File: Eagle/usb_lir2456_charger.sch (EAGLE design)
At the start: 14 parts

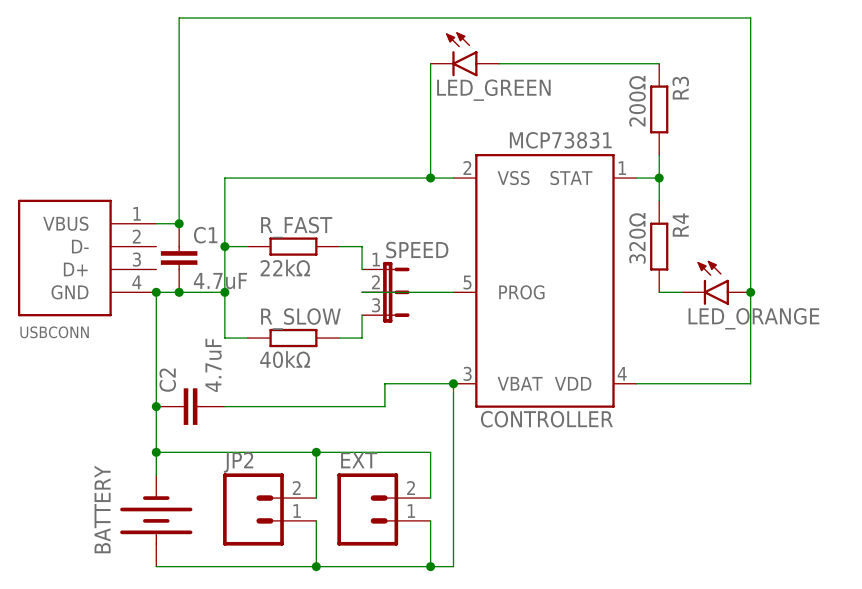
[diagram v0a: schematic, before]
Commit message: Edited Charge and Done Led connections
actually I have not able to test it is it correct or not. How ever next week i will be able to do it. Before it maybe some one could have chance before me. Best regards.  Note: I have get the idea from https://www.electroschematics.com/3-7v-li-ion-battery-charger-circuit/ that link.
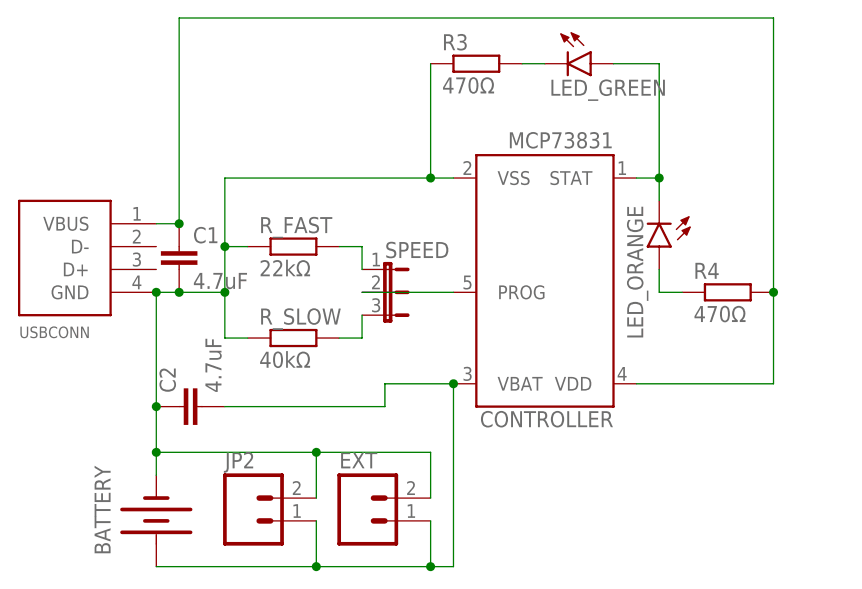
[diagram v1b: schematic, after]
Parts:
- R3: value 200Ω -> 470Ω
- R4: value 320Ω -> 470Ω
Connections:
- net GND: now also R3.1; no longer LED_GREEN.C
- net N$1: now also LED_GREEN.A, LED_ORANGE.C; no longer R3.2, R4.1
- net N$4: now also LED_GREEN.C, R3.2; no longer LED_GREEN.A, R3.1
- net N$7: now also LED_ORANGE.A, R4.1; no longer LED_ORANGE.C, R4.2
- net VCC: now also R4.2; no longer LED_ORANGE.A
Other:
- moved on the sheet: LED_GREEN, LED_ORANGE, R3, R4
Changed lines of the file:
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@@
 <?xml version="1.0" encoding="utf-8"?>
 <!DOCTYPE eagle SYSTEM "eagle.dtd">
-<eagle version="6.5.0">
+<eagle version="9.6.2">
 <drawing>
 <settings>
 <setting alwaysvectorfont="no"/>
+<setting keepoldvectorfont="yes"/>
 <setting verticaltext="up"/>
 </settings>
@@
 <part name="R_SLOW" library="eagle-ltspice" deviceset="R" device="" value="40kΩ"/>
 <part name="R_FAST" library="eagle-ltspice" deviceset="R" device="" value="22kΩ"/>
-<part name="R3" library="eagle-ltspice" deviceset="R" device="" value="200Ω"/>
-<part name="R4" library="eagle-ltspice" deviceset="R" device="" value="320Ω"/>
-<part name="LED_ORANGE" library="SparkFun-LED" deviceset="LED" device="0603"/>
-<part name="LED_GREEN" library="SparkFun-LED" deviceset="LED" device="0603"/>
 <part name="BATTERY" library="SparkFun-Electromechanical" deviceset="BATTERY" device="20PTH"/>
 <part name="SPEED" library="jumper" deviceset="JP2E" device=""/>
 <part name="JP2" library="SparkFun-Connectors" deviceset="M02" device="JST-PTH-VERT" value=""/>
 <part name="EXT" library="SparkFun-Connectors" deviceset="M02" device="PTH" value=""/>
+<part name="R4" library="eagle-ltspice" deviceset="R" device="" value="470Ω"/>
+<part name="LED_ORANGE" library="SparkFun-LED" deviceset="LED" device="0603"/>
+<part name="LED_GREEN" library="SparkFun-LED" deviceset="LED" device="0603"/>
+<part name="R3" library="eagle-ltspice" deviceset="R" device="" value="470Ω"/>
 </parts>
 <sheets>
@@
 </plain>
 <instances>
-<instance part="CONTROLLER" gate="G$1" x="114.3" y="104.14" rot="R180"/>
-<instance part="USBCONN" gate="G$1" x="60.96" y="104.14"/>
-<instance part="C1" gate="G$1" x="73.66" y="109.22"/>
-<instance part="C2" gate="G$1" x="73.66" y="91.44" rot="R90"/>
-<instance part="R_SLOW" gate="G$1" x="86.36" y="99.06"/>
-<instance part="R_FAST" gate="G$1" x="86.36" y="109.22"/>
-<instance part="R3" gate="G$1" x="127" y="124.46" rot="R270"/>
-<instance part="R4" gate="G$1" x="127" y="109.22" rot="R270"/>
-<instance part="LED_ORANGE" gate="G$1" x="134.62" y="104.14" rot="R270"/>
-<instance part="LED_GREEN" gate="G$1" x="106.68" y="129.54" rot="R270"/>
-<instance part="BATTERY" gate="G$1" x="71.12" y="78.74" rot="R90"/>
-<instance part="SPEED" gate="1" x="96.52" y="104.14" rot="R270"/>
-<instance part="JP2" gate="G$1" x="81.28" y="78.74"/>
-<instance part="EXT" gate="G$1" x="93.98" y="78.74"/>
+<instance part="CONTROLLER" gate="G$1" x="114.3" y="104.14" smashed="yes" rot="R180">
+<attribute name="NAME" x="121.92" y="90.932" size="1.778" layer="95" rot="R180"/>
+<attribute name="VALUE" x="121.92" y="121.92" size="1.778" layer="96" rot="R180"/>
+</instance>
+<instance part="USBCONN" gate="G$1" x="60.96" y="104.14" smashed="yes">
+<attribute name="NAME" x="55.88" y="99.06" size="1.27" layer="95"/>
+</instance>
+<instance part="C1" gate="G$1" x="73.66" y="109.22" smashed="yes">
+<attribute name="NAME" x="75.184" y="109.601" size="1.778" layer="95"/>
+<attribute name="VALUE" x="75.184" y="104.521" size="1.778" layer="96"/>
+</instance>
+<instance part="C2" gate="G$1" x="73.66" y="91.44" smashed="yes" rot="R90">
+<attribute name="NAME" x="73.279" y="92.964" size="1.778" layer="95" rot="R90"/>
+<attribute name="VALUE" x="78.359" y="92.964" size="1.778" layer="96" rot="R90"/>
+</instance>
+<instance part="R_SLOW" gate="G$1" x="86.36" y="99.06" smashed="yes">
+<attribute name="NAME" x="82.55" y="100.5586" size="1.778" layer="95"/>
+<attribute name="VALUE" x="82.55" y="95.758" size="1.778" layer="96"/>
+</instance>
+<instance part="R_FAST" gate="G$1" x="86.36" y="109.22" smashed="yes">
+<attribute name="NAME" x="82.55" y="110.7186" size="1.778" layer="95"/>
+<attribute name="VALUE" x="82.55" y="105.918" size="1.778" layer="96"/>
+</instance>
+<instance part="BATTERY" gate="G$1" x="71.12" y="78.74" smashed="yes" rot="R90">
+<attribute name="NAME" x="66.04" y="74.93" size="1.778" layer="95" rot="R90"/>
+<attribute name="VALUE" x="77.47" y="74.93" size="1.778" layer="96" rot="R90"/>
+</instance>
+<instance part="SPEED" gate="1" x="96.52" y="104.14" smashed="yes" rot="R270">
+<attribute name="NAME" x="96.52" y="107.95" size="1.778" layer="95"/>
+<attribute name="VALUE" x="96.52" y="98.425" size="1.778" layer="96"/>
+</instance>
+<instance part="JP2" gate="G$1" x="81.28" y="78.74" smashed="yes">
+<attribute name="VALUE" x="78.74" y="73.66" size="1.778" layer="96"/>
+<attribute name="NAME" x="78.74" y="84.582" size="1.778" layer="95"/>
+</instance>
+<instance part="EXT" gate="G$1" x="93.98" y="78.74" smashed="yes">
+<attribute name="VALUE" x="91.44" y="73.66" size="1.778" layer="96"/>
+<attribute name="NAME" x="91.44" y="84.582" size="1.778" layer="95"/>
+</instance>
+<instance part="R4" gate="G$1" x="134.62" y="104.14" smashed="yes">
+<attribute name="NAME" x="130.81" y="105.6386" size="1.778" layer="95"/>
+<attribute name="VALUE" x="130.81" y="100.838" size="1.778" layer="96"/>
+</instance>
+<instance part="LED_ORANGE" gate="G$1" x="127" y="109.22" smashed="yes" rot="R180">
+<attribute name="NAME" x="123.444" y="113.792" size="1.778" layer="95" rot="R270"/>
+<attribute name="VALUE" x="121.285" y="113.792" size="1.778" layer="96" rot="R270"/>
+</instance>
+<instance part="LED_GREEN" gate="G$1" x="119.38" y="129.54" smashed="yes" rot="R270">
+<attribute name="NAME" x="114.808" y="125.984" size="1.778" layer="95"/>
+<attribute name="VALUE" x="114.808" y="123.825" size="1.778" layer="96"/>
+</instance>
+<instance part="R3" gate="G$1" x="106.68" y="129.54" smashed="yes">
+<attribute name="NAME" x="102.87" y="131.0386" size="1.778" layer="95"/>
+<attribute name="VALUE" x="102.87" y="126.238" size="1.778" layer="96"/>
+</instance>
 </instances>
 <busses>
@@
 <pinref part="CONTROLLER" gate="G$1" pin="VSS"/>
 <wire x1="78.74" y1="116.84" x2="101.6" y2="116.84" width="0.1524" layer="91"/>
-<pinref part="LED_GREEN" gate="G$1" pin="C"/>
 <wire x1="101.6" y1="116.84" x2="104.14" y2="116.84" width="0.1524" layer="91"/>
 <wire x1="101.6" y1="129.54" x2="101.6" y2="116.84" width="0.1524" layer="91"/>
 <junction x="101.6" y="116.84"/>
+<pinref part="R3" gate="G$1" pin="1"/>
 </segment>
 </net>
@@
 <net name="N$4" class="0">
 <segment>
-<pinref part="R3" gate="G$1" pin="1"/>
-<pinref part="LED_GREEN" gate="G$1" pin="A"/>
-<wire x1="127" y1="129.54" x2="109.22" y2="129.54" width="0.1524" layer="91"/>
+<wire x1="114.3" y1="129.54" x2="111.76" y2="129.54" width="0.1524" layer="91"/>
+<pinref part="R3" gate="G$1" pin="2"/>
+<pinref part="LED_GREEN" gate="G$1" pin="C"/>
 </segment>
 </net>
 <net name="N$7" class="0">
 <segment>
-<pinref part="R4" gate="G$1" pin="2"/>
-<pinref part="LED_ORANGE" gate="G$1" pin="C"/>
 <wire x1="127" y1="104.14" x2="129.54" y2="104.14" width="0.1524" layer="91"/>
+<pinref part="R4" gate="G$1" pin="1"/>
+<pinref part="LED_ORANGE" gate="G$1" pin="A"/>
+<wire x1="127" y1="104.14" x2="127" y2="106.68" width="0.1524" layer="91"/>
 </segment>
 </net>
 <net name="VCC" class="0">
 <segment>
-<wire x1="137.16" y1="134.62" x2="73.66" y2="134.62" width="0.1524" layer="91"/>
+<wire x1="139.7" y1="134.62" x2="73.66" y2="134.62" width="0.1524" layer="91"/>
 <pinref part="USBCONN" gate="G$1" pin="VBUS"/>
 <pinref part="C1" gate="G$1" pin="1"/>
@@
 <junction x="73.66" y="111.76"/>
 <pinref part="CONTROLLER" gate="G$1" pin="VDD"/>
-<wire x1="137.16" y1="93.98" x2="124.46" y2="93.98" width="0.1524" layer="91"/>
-<pinref part="LED_ORANGE" gate="G$1" pin="A"/>
-<wire x1="137.16" y1="93.98" x2="137.16" y2="104.14" width="0.1524" layer="91"/>
-<wire x1="137.16" y1="104.14" x2="137.16" y2="134.62" width="0.1524" layer="91"/>
-<junction x="137.16" y="104.14"/>
+<wire x1="139.7" y1="93.98" x2="124.46" y2="93.98" width="0.1524" layer="91"/>
+<wire x1="139.7" y1="93.98" x2="139.7" y2="104.14" width="0.1524" layer="91"/>
+<pinref part="R4" gate="G$1" pin="2"/>
+<wire x1="139.7" y1="104.14" x2="139.7" y2="134.62" width="0.1524" layer="91"/>
+<junction x="139.7" y="104.14"/>
 </segment>
 </net>
@@
 <net name="N$1" class="0">
 <segment>
-<pinref part="R3" gate="G$1" pin="2"/>
-<pinref part="R4" gate="G$1" pin="1"/>
-<wire x1="127" y1="119.38" x2="127" y2="116.84" width="0.1524" layer="91"/>
 <pinref part="CONTROLLER" gate="G$1" pin="STAT"/>
 <wire x1="127" y1="116.84" x2="127" y2="114.3" width="0.1524" layer="91"/>
 <wire x1="124.46" y1="116.84" x2="127" y2="116.84" width="0.1524" layer="91"/>
 <junction x="127" y="116.84"/>
-</segment>
-</net>
+<pinref part="LED_ORANGE" gate="G$1" pin="C"/>
+<pinref part="LED_GREEN" gate="G$1" pin="A"/>
+<wire x1="127" y1="116.84" x2="127" y2="129.54" width="0.1524" layer="91"/>
+<wire x1="127" y1="129.54" x2="121.92" y2="129.54" width="0.1524" layer="91"/>
+</segment>
+</net>
